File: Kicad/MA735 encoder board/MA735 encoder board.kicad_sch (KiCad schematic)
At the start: 5 parts, among them J2 JST SH SM06B, U1 MA735GGU-Z

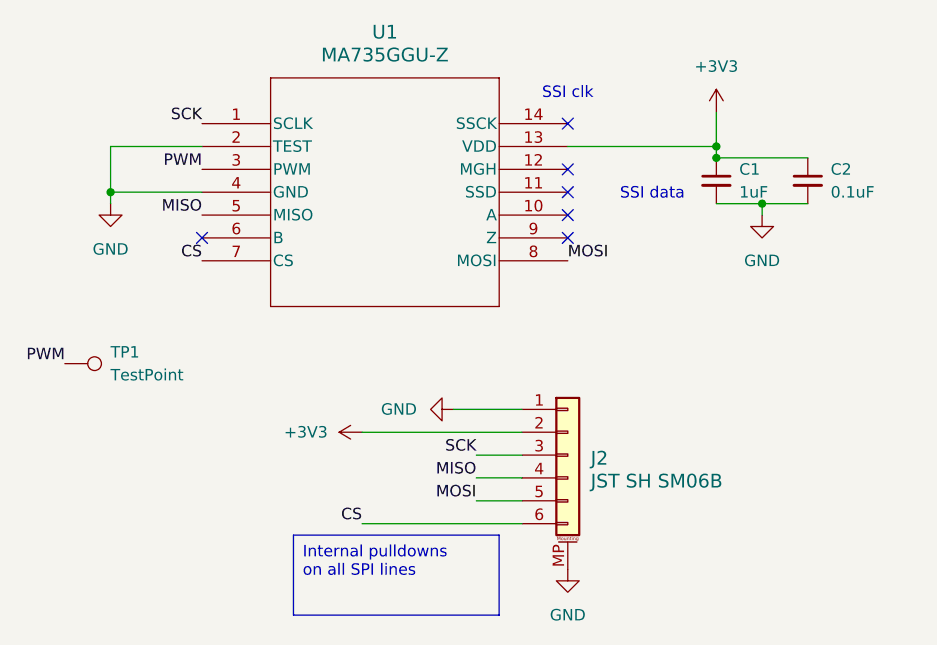
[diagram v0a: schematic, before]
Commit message: Start redesign of encoder board for flex circuit
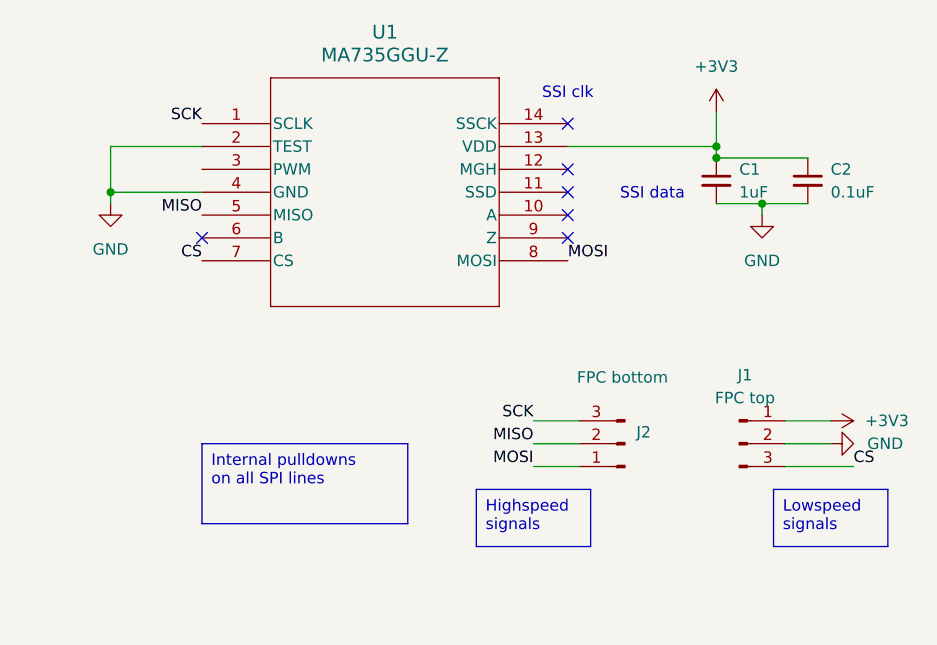
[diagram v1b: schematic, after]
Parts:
- removed J2: JST SH SM06B, Connector_JST:JST_SH_SM06B-SRSS-TB_1x06-1MP_P1.00mm_Horizontal, symbol Connector_Generic_MountingPin:Conn_01x06_MountingPin
- removed TP1: TestPoint, TestPoint:TestPoint_Pad_D2.0mm, symbol Connector:TestPoint
- added J1: FPC top, symbol Connector:Conn_01x03_Pin
- added J2: FPC bottom, symbol Connector:Conn_01x03_Pin
- C1, C2: footprint Capacitor_SMD:C_0603_1608Metric -> Capacitor_SMD:C_0402_1005Metric
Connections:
- net +3V3: now also J1.1 (Pin_1)
- net CS: now also J1.3 (Pin_3)
- net GND: now also J1.2 (Pin_2)
- net MISO: now also J2.2 (Pin_2)
- net MOSI: now also J2.1 (Pin_1)
- net SCK: now also J2.3 (Pin_3)
- net PWM: no longer names the net of U1.3 (PWM)

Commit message: Partial layout complete
I currently have the board sized at 4.5mm with a really long cable. This is probably WAY to small, I can barely fit the 0402 capacitors.
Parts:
- J1, J2: footprint (none) -> custom_testpoints:3pin_fpc
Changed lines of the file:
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@@
 			)
 		)
-		(property "Footprint" ""
+		(property "Footprint" "custom_testpoints:3pin_fpc"
 			(at 167.64 113.03 0)
 			(effects
@@
 			)
 		)
-		(property "Footprint" ""
+		(property "Footprint" "custom_testpoints:3pin_fpc"
 			(at 180.34 113.03 0)
 			(effects

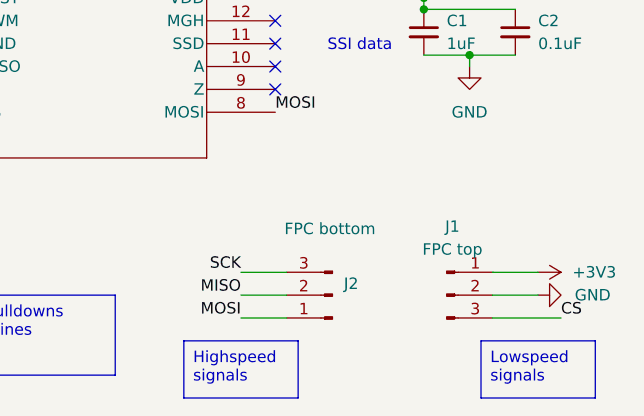
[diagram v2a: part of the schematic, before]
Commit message: Finished 7pin fpc contacts
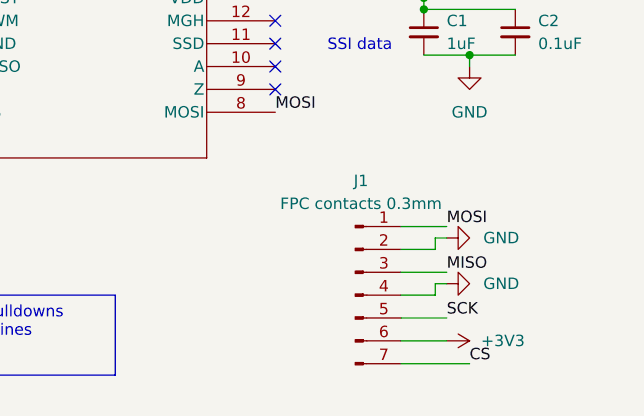
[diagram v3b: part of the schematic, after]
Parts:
- removed J1: FPC top, custom_testpoints:3pin_fpc, symbol Connector:Conn_01x03_Pin
- removed J2: FPC bottom, custom_testpoints:3pin_fpc, symbol Connector:Conn_01x03_Pin
- added J1: FPC contacts 0.3mm, custom_testpoints:7pin_fpc_contact_0.3mmptich, symbol Connector:Conn_01x07_Pin
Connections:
- net +3V3: now also J1.6 (Pin_6)
- net CS: now also J1.7 (Pin_7)
- net GND: now also J1.2 (Pin_2), J1.4 (Pin_4)
- net MISO: now also J1.3 (Pin_3)
- net MOSI: now also J1.1 (Pin_1)
- net SCK: now also J1.5 (Pin_5)
